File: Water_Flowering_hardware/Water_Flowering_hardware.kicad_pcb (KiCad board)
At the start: 2 copper layers, 72.2 x 36.4 mm, 19 parts, among them J1 Water_Level_Sensor_Module, J2 Soil_Moisture_Sensor_Module, J3 Conn_01x02, J4 Power Jack, K1 Relay_SPDT, Q1 MMBT5550L, U1 CD74HC4067SM, U2 WeMos_D1_mini, U3 LM1117MP-3.3, U4 LM1117MP-5.0

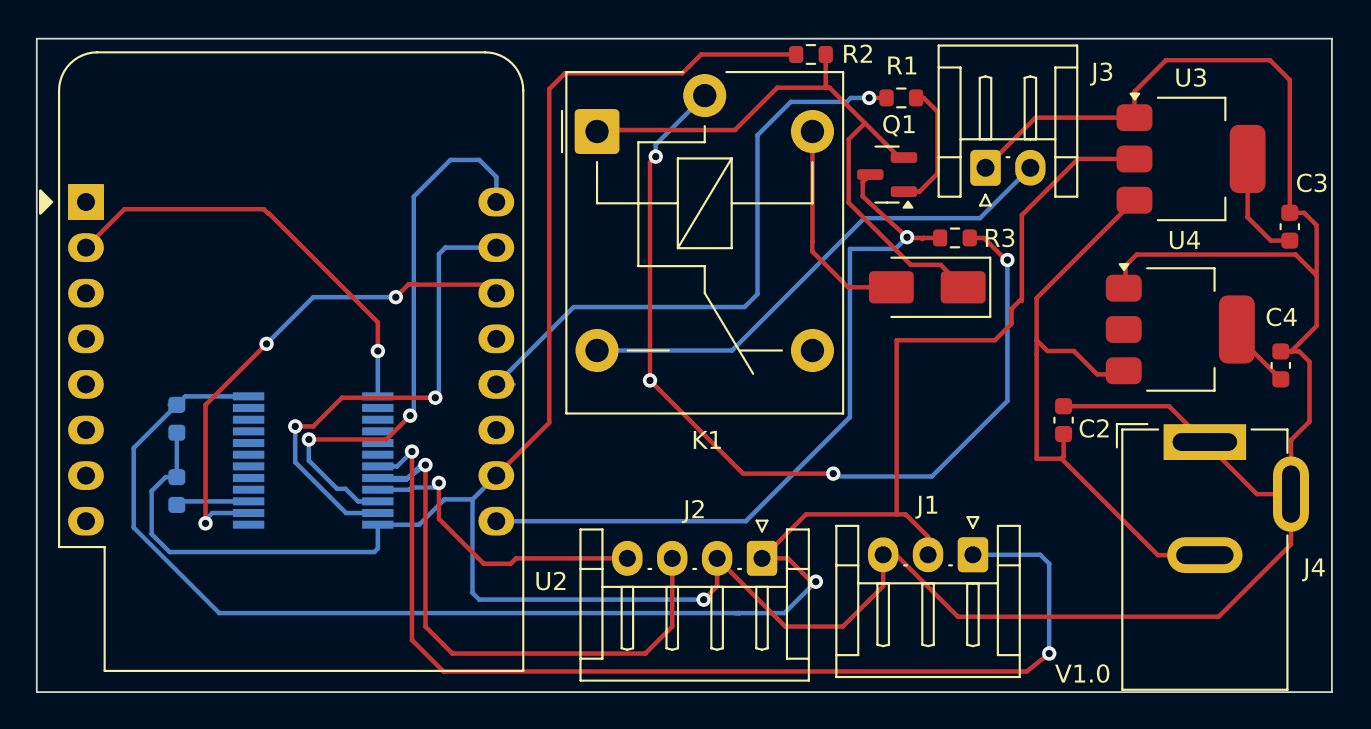
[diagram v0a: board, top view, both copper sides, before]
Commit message: Fix: 修正JACK的VIN和GND腳位和走線和修正5V的走線
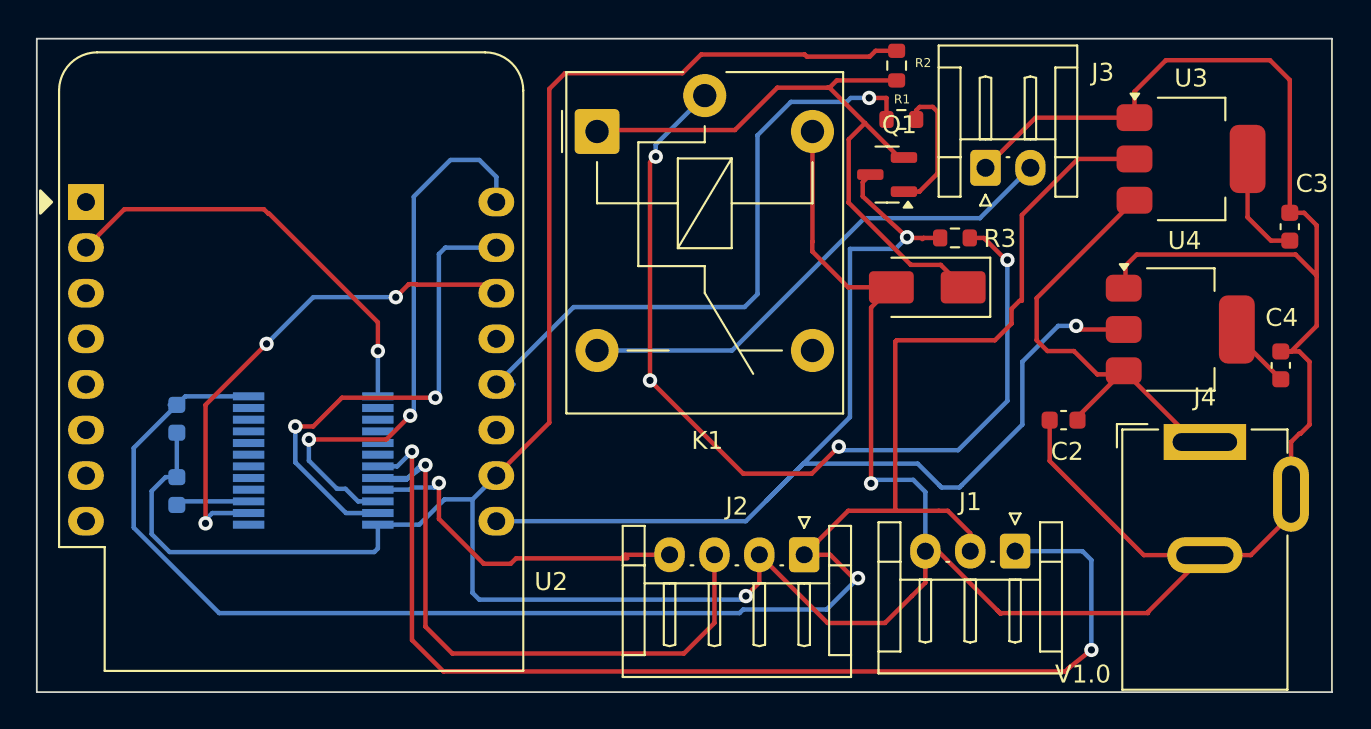
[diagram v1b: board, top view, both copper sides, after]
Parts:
- moved R2 4.82 mm to (182.5, 99.5), turned to -90 degrees
- moved J1 2.36 mm to (189.1, 126.5)
- moved J2 2.36 mm to (177.3, 126.8)
- moved R1 1.20 mm to (182.8, 102.5)
- turned C2 to 180 degrees
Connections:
- J4 pad 1: /GND -> /VIN
- J4 pad 2: /VIN -> /GND
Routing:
- net /5V: track 46.0 -> 73.5 mm, vias 1 -> 2
- net /GND: track 215.8 -> 238.4 mm, vias 1 -> 2
- net /VIN: track 35.7 -> 26.1 mm
- net /Soil_A0: track 17.2 -> 20.0 mm
- net /W0: track 59.0 -> 61.5 mm
- net /Soil_D0: track 33.1 -> 35.6 mm
- net Net-(D1-K): track 35.4 -> 37.4 mm
- net /3.3V: track 105.2 -> 107.3 mm
- net /Water_Out: track 34.6 -> 35.8 mm

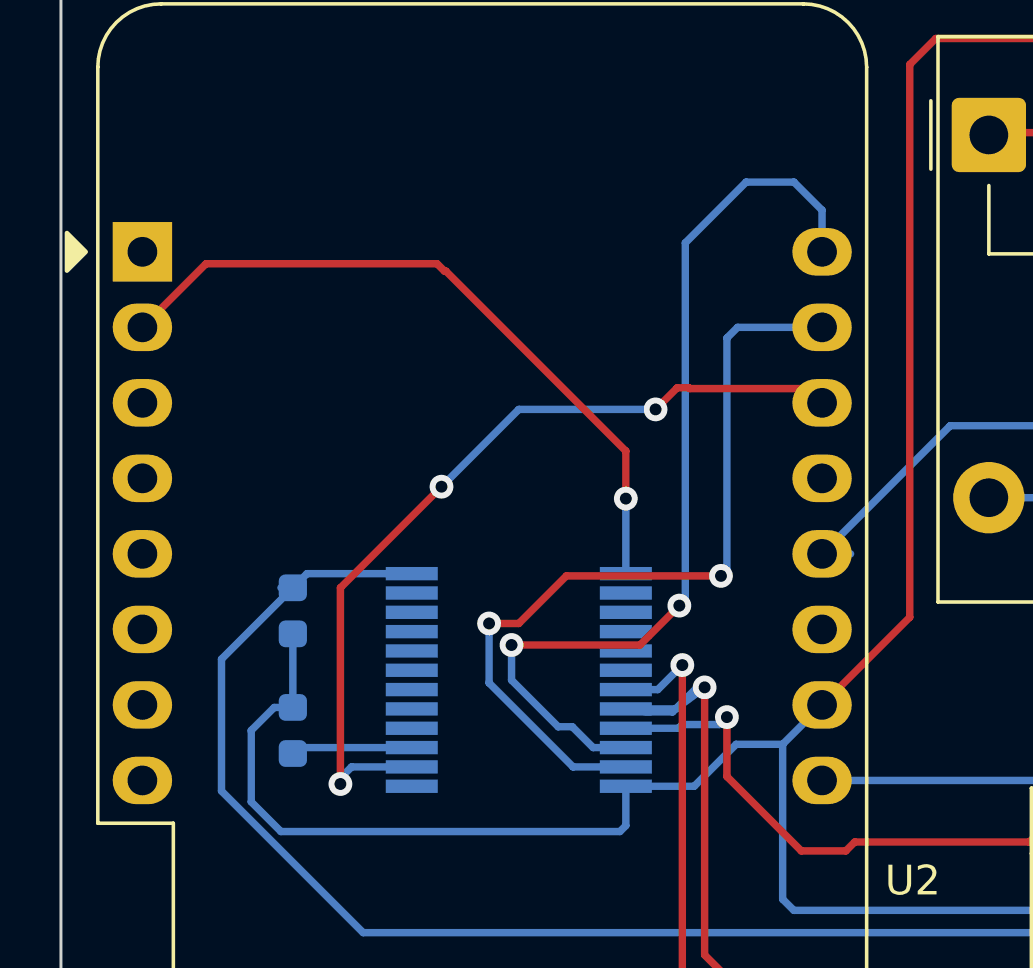
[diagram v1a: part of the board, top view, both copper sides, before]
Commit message: Fix: 確認CD74HC4067功能後並修正相對的GPIO腳位
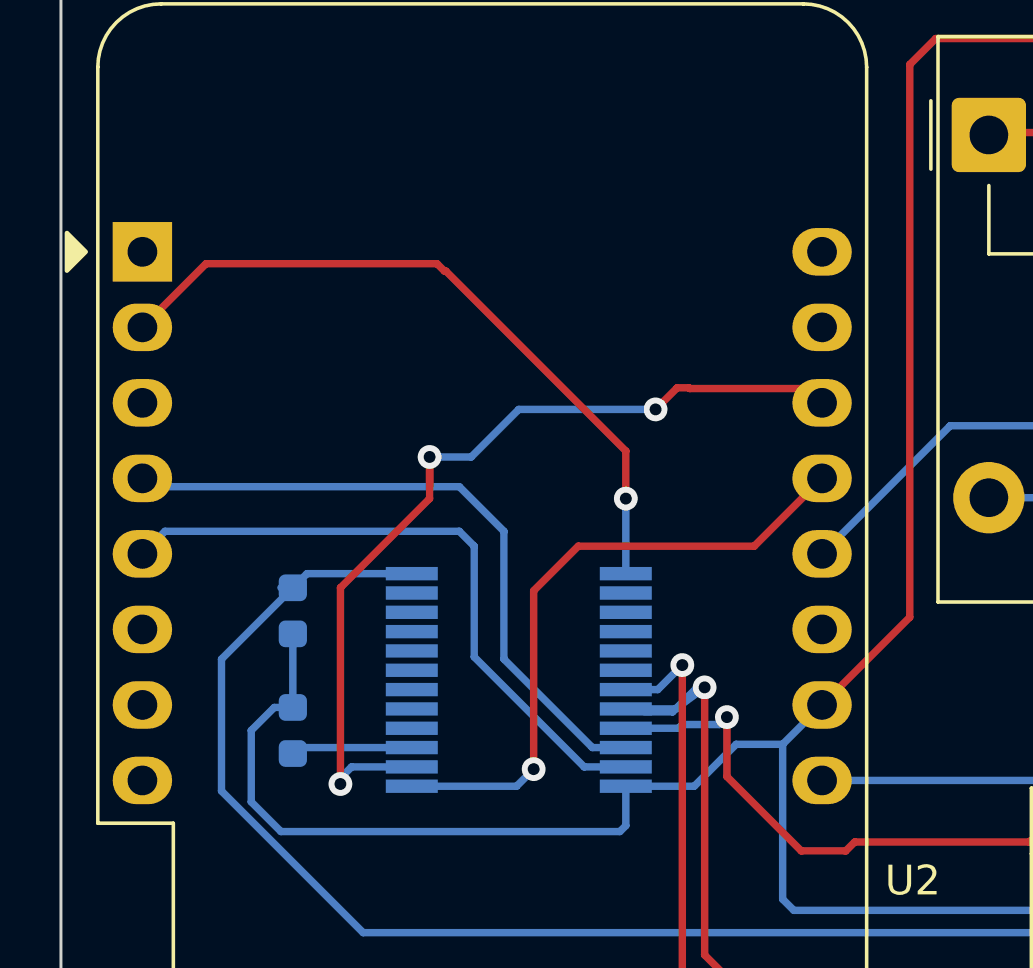
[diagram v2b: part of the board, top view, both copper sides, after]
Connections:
- U2 pad 13: /S4 -> /S3
- U2 pad 15: /S1 -> unconnected-(U2-RX-Pad15)
- U2 pad 16: /S0 -> unconnected-(U2-TX-Pad16)
- U2 pad 4: unconnected-(U2-SCK/D5-Pad4) -> /S0
- U2 pad 5: unconnected-(U2-MISO/D6-Pad5) -> /S1
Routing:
- net /S3: track 0.00 -> 21.6 mm, vias 0 -> 1
- net /S0: track 31.7 -> 22.5 mm, vias 2 -> 0
- net /S1: track 27.9 -> 22.0 mm, vias 2 -> 0
- net /S2: track 29.0 -> 30.6 mm
- net /Water_Out: track 35.8 -> 34.9 mm

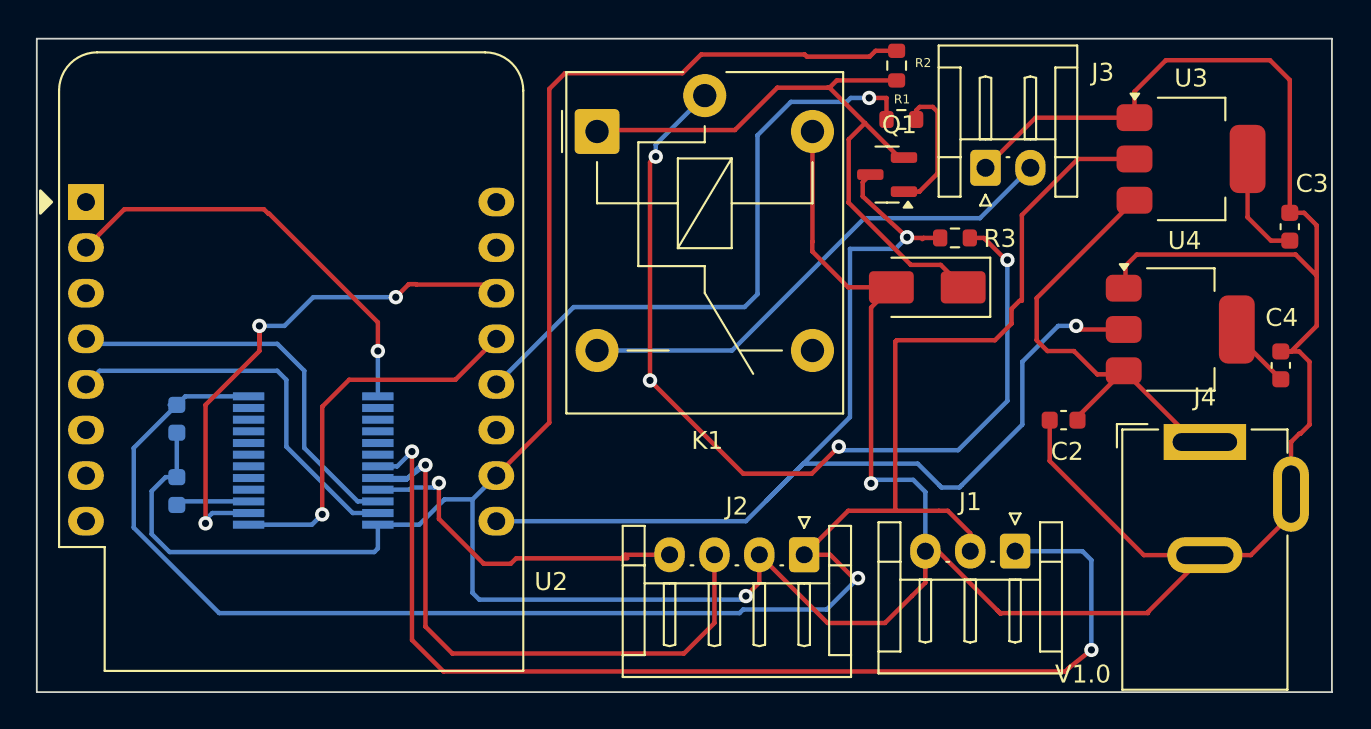
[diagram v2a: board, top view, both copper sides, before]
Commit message: Feat: 加入APSTA腳位到D0腳位 - 原本為pull high可進入一種模式(STA或AP)，可透過短路2PIN接地進入另一種模式
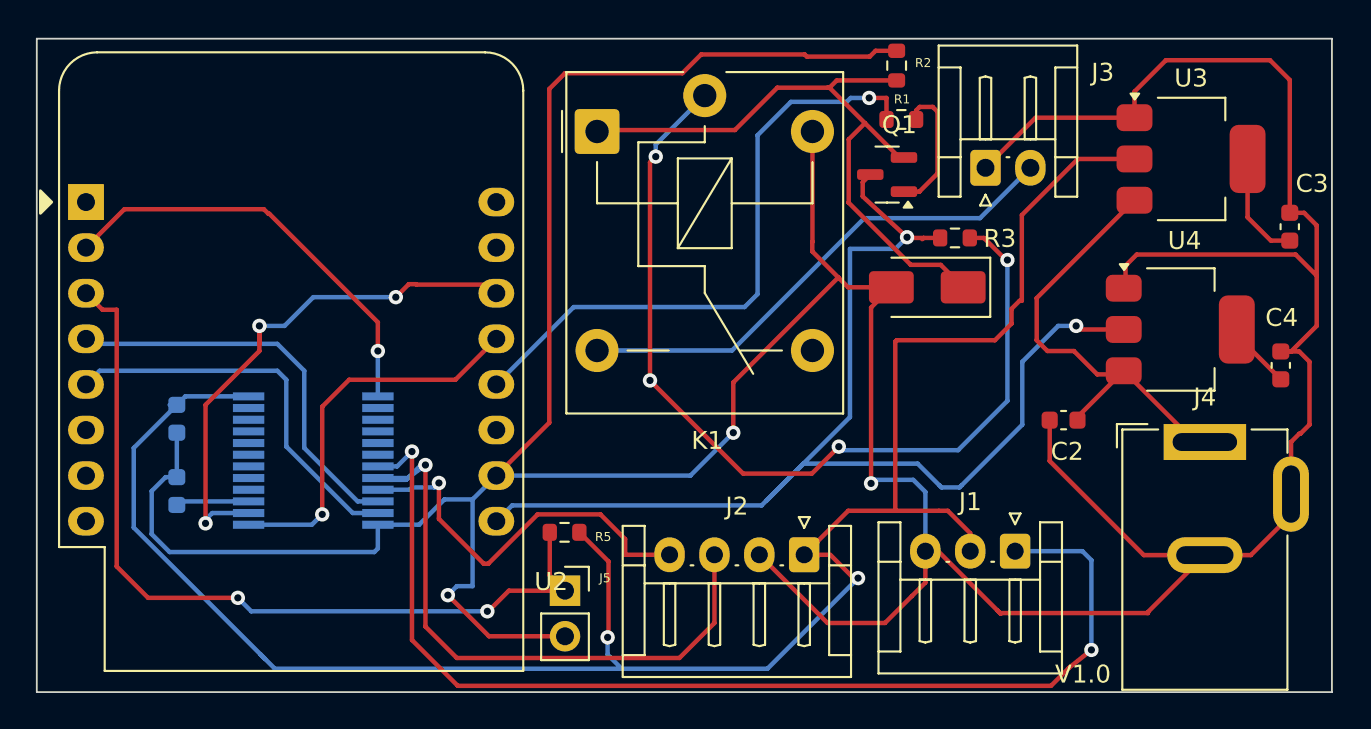
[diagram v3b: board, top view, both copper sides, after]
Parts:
- added J5: Conn_01x02, Connector_PinSocket_2.54mm:PinSocket_1x02_P2.54mm_Vertical, F.Cu at (164.0, 128.8)
- added R5: 10k, Resistor_SMD:R_0603_1608Metric, F.Cu at (164.0, 125.5)
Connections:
- U2 pad 3: unconnected-(U2-D0-Pad3) -> /APSTA_SEL
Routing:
- net /APSTA_SEL: track 0.00 -> 46.7 mm, vias 0 -> 2
- net /GND: track 238.4 -> 254.1 mm, vias 2 -> 3
- net /3.3V: track 107.3 -> 118.8 mm, vias 1 -> 2
- net /Soil_A0: track 20.0 -> 22.0 mm
- net /W0: track 61.5 -> 62.1 mm

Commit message: Fix: 修正繼電器控制電路 - 加入準位轉換電路(3.3V-5V) - 修正繼電器控制腳位 - 結合準位轉換電路以及用5V輸出準位控制繼電器電路
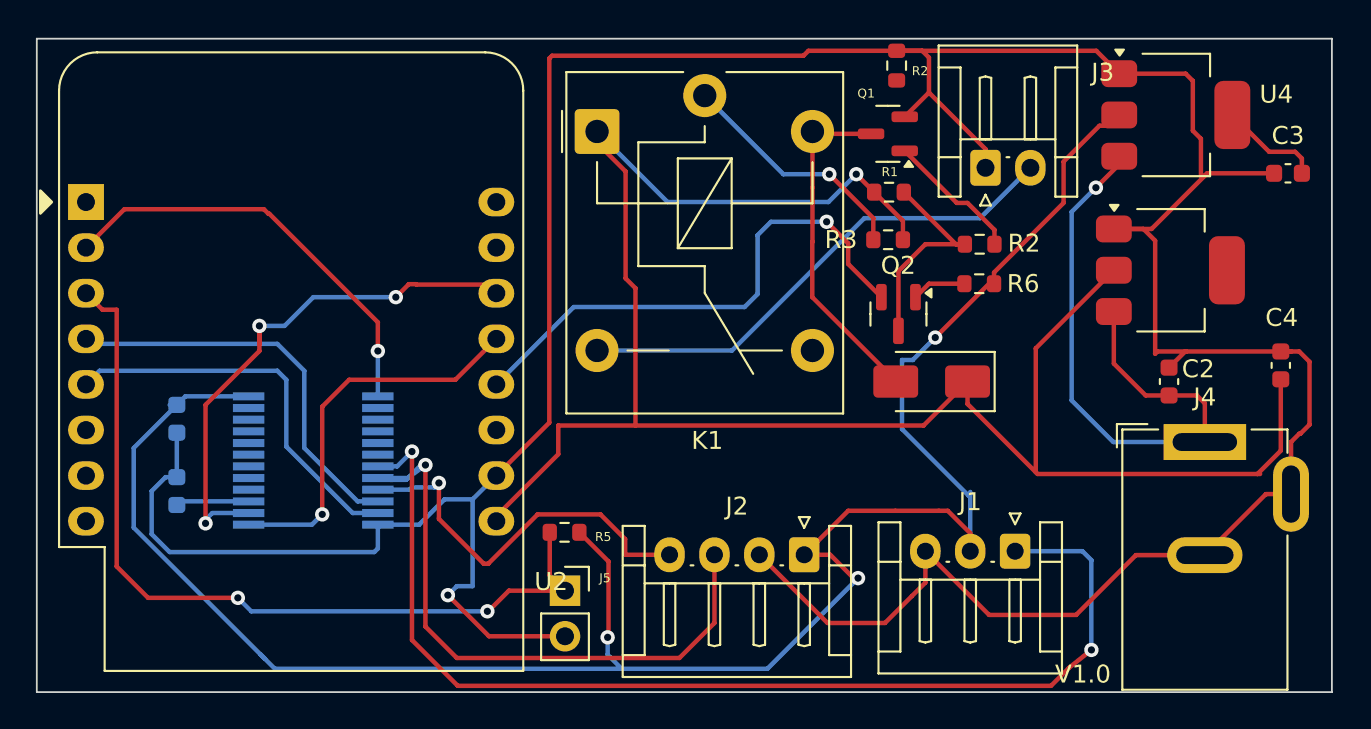
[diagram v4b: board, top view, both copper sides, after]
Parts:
- added Q2: MMBT5550L, Package_TO_SOT_SMD:SOT-23, F.Cu at (182.6, 113.3)
- added R2: 1k, Resistor_SMD:R_0603_1608Metric, F.Cu at (187.1, 109.5)
- added R6: 1k, Resistor_SMD:R_0603_1608Metric, F.Cu at (187.1, 111.7)
- moved C2 6.26 mm to (197.7, 117.1), turned to 90 degrees
- moved D1 5.26 mm to (184.4, 117.1)
- moved R1 4.11 mm to (182.1, 106.5)
- moved R3 3.73 mm to (182.0, 109.2), turned to 180 degrees
- moved U4 3.35 mm to (197.8, 110.9)
- moved C3 2.98 mm to (204.3, 105.5), turned to 180 degrees
- moved U3 2.59 mm to (198.1, 102.2)
- moved Q1 2.27 mm to (182.0, 103.3)
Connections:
- D1 pad 1: Net-(D1-K) -> /5V
- D1 pad 2: /GND -> Net-(D1-A)
- K1 pad A1: Net-(D1-K) -> /5V
- K1 pad A2: /GND -> Net-(D1-A)
- Q1 pad 2: Net-(D1-K) -> /GND
- Q1 pad 3: /5V -> Net-(D1-A)
- R1 pad 1: /Water_Out -> /5V
- R1 pad 2: Net-(Q1-B) -> Net-(Q2-C)
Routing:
- net /GND: track 254.1 -> 198.8 mm, vias 3 -> 1
- net Net-(K1-Pad11): track 51.6 -> 13.4 mm, vias 4 -> 1
- net Net-(D1-K): track 37.4 -> 0.00 mm
- net /5V: track 73.5 -> 107.6 mm, vias 2 -> 1
- net Net-(D1-A): track 0.00 -> 19.0 mm
- net Net-(Q2-C): track 0.00 -> 12.2 mm
- net /VIN: track 26.1 -> 34.9 mm, vias 0 -> 1
- net /Water_Out: track 34.9 -> 29.5 mm
- net Net-(Q2-B): track 0.00 -> 3.04 mm
- net /3.3V: track 118.8 -> 119.9 mm, vias 2 -> 3
